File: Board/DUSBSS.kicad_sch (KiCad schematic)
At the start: 8 parts, among them Q2 BC857, U5 AP22652W6-7

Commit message: Finished Schematic
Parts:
- C2, C3: footprint (none) -> Capacitor_SMD:C_0603_1608Metric
- R19: renamed from R16; footprint (none) -> Resistor_SMD:R_0603_1608Metric
- R5, R6, R7: footprint (none) -> Resistor_SMD:R_0603_1608Metric
- U5: footprint SOIC_52W6-7_DIO -> Library:SOIC_52W6-7_DIO
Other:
- sheet USB_C0 ports: added A0, A1; removed none
- sheet USB_C1 ports: added A0, A1; removed none
- note added: "Protection and Detection"
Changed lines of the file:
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@@
 	(generator_version "9.0")
 	(paper "A4")
+	(text "Protection and Detection"
+		(exclude_from_sim no)
+		(at 152.146 155.194 0)
+		(effects
+			(font
+				(size 2.45 2.45)
+				(thickness 0.49)
+				(bold yes)
+			)
+		)
+	)
 	(junction
 		(at 125.73 125.73)
@@
 		)
 	)
+	(bus
+		(pts
+			(xy 193.04 64.77) (xy 193.04 157.48)
+		)
+		(stroke
+			(width 0)
+			(type default)
+		)
+	)
 	(wire
 		(pts
@@
 		)
 	)
+	(bus
+		(pts
+			(xy 111.76 64.77) (xy 193.04 64.77)
+		)
+		(stroke
+			(width 0)
+			(type default)
+		)
+	)
 	(wire
 		(pts
@@
 		)
 	)
+	(bus
+		(pts
+			(xy 111.76 157.48) (xy 111.76 64.77)
+		)
+		(stroke
+			(width 0)
+			(type default)
+		)
+	)
 	(wire
 		(pts
@@
 		(pts
 			(xy 153.67 102.87) (xy 153.67 130.81)
+		)
+		(stroke
+			(width 0)
+			(type default)
+		)
+	)
+	(bus
+		(pts
+			(xy 193.04 157.48) (xy 111.76 157.48)
 		)
 		(stroke
@@
 		)
 	)
+	(hierarchical_label "A10"
+		(shape bidirectional)
+		(at 186.69 128.27 0)
+		(effects
+			(font
+				(size 1.27 1.27)
+			)
+			(justify left)
+		)
+	)
 	(hierarchical_label "FAULT"
 		(shape output)
@@
 			)
 			(justify right)
+		)
+	)
+	(hierarchical_label "A01"
+		(shape bidirectional)
+		(at 186.69 97.79 0)
+		(effects
+			(font
+				(size 1.27 1.27)
+			)
+			(justify left)
+		)
+	)
+	(hierarchical_label "A11"
+		(shape bidirectional)
+		(at 186.69 125.73 0)
+		(effects
+			(font
+				(size 1.27 1.27)
+			)
+			(justify left)
+		)
+	)
+	(hierarchical_label "A00"
+		(shape bidirectional)
+		(at 186.69 100.33 0)
+		(effects
+			(font
+				(size 1.27 1.27)
+			)
+			(justify left)
 		)
 	)
@@
 			)
 		)
-		(property "Footprint" ""
+		(property "Footprint" "Resistor_SMD:R_0603_1608Metric"
 			(at 120.65 76.962 90)
 			(effects
@@
 				)
 				(path "/06ff9557-1f9b-4670-8a34-bb7684a016dd/21559adc-22f0-4da5-bb39-da22b4a6076e"
-					(reference "R10")
+					(reference "R12")
 					(unit 1)
 				)
 				(path "/06ff9557-1f9b-4670-8a34-bb7684a016dd/2b86b0ae-2209-4a30-98e5-d26e75080e9f"
-					(reference "R12")
+					(reference "R15")
 					(unit 1)
 				)
 				(path "/06ff9557-1f9b-4670-8a34-bb7684a016dd/c6b53444-adaa-455c-990e-02e7d6acd668"
-					(reference "R8")
+					(reference "R9")
 					(unit 1)
 				)
@@
 			)
 		)
-		(property "Footprint" ""
+		(property "Footprint" "Resistor_SMD:R_0603_1608Metric"
 			(at 141.732 110.49 90)
 			(effects
@@
 				)
 				(path "/06ff9557-1f9b-4670-8a34-bb7684a016dd/21559adc-22f0-4da5-bb39-da22b4a6076e"
-					(reference "R11")
+					(reference "R13")
 					(unit 1)
 				)
 				(path "/06ff9557-1f9b-4670-8a34-bb7684a016dd/2b86b0ae-2209-4a30-98e5-d26e75080e9f"
-					(reference "R13")
+					(reference "R16")
 					(unit 1)
 				)
 				(path "/06ff9557-1f9b-4670-8a34-bb7684a016dd/c6b53444-adaa-455c-990e-02e7d6acd668"
-					(reference "R9")
+					(reference "R10")
 					(unit 1)
 				)
@@
 		(dnp no)
 		(fields_autoplaced yes)
-		(property "Reference" "#PWR?"
+		(property "Reference" "#PWR0101"
 			(at 138.43 128.27 0)
 			(effects
@@
 			(project "SlimeVR_Dock"
 				(path "/06ff9557-1f9b-4670-8a34-bb7684a016dd/20608bd6-1177-4976-ba2c-965ba6250d58"
-					(reference "#PWR?")
+					(reference "#PWR0101")
 					(unit 1)
 				)
@@
 			)
 		)
-		(property "Footprint" ""
+		(property "Footprint" "Capacitor_SMD:C_0603_1608Metric"
 			(at 182.5752 88.9 0)
 			(effects
@@
 			)
 		)
-		(property "Footprint" ""
+		(property "Footprint" "Capacitor_SMD:C_0603_1608Metric"
 			(at 129.2352 93.98 0)
 			(effects
@@
 			)
 		)
-		(property "Footprint" ""
+		(property "Footprint" "Resistor_SMD:R_0603_1608Metric"
 			(at 123.952 130.81 90)
 			(effects
@@
 				)
 				(path "/06ff9557-1f9b-4670-8a34-bb7684a016dd/21559adc-22f0-4da5-bb39-da22b4a6076e"
-					(reference "R10")
+					(reference "R11")
 					(unit 1)
 				)
 				(path "/06ff9557-1f9b-4670-8a34-bb7684a016dd/2b86b0ae-2209-4a30-98e5-d26e75080e9f"
-					(reference "R11")
+					(reference "R14")
 					(unit 1)
 				)
@@
 		(on_board yes)
 		(dnp no)
-		(property "Reference" "R16"
+		(property "Reference" "R19"
 			(at 135.128 146.05 0)
 			(effects
@@
 			)
 		)
-		(property "Footprint" ""
+		(property "Footprint" "Resistor_SMD:R_0603_1608Metric"
 			(at 139.192 147.32 90)
 			(effects
@@
 			(project "SlimeVR_Dock"
 				(path "/06ff9557-1f9b-4670-8a34-bb7684a016dd/20608bd6-1177-4976-ba2c-965ba6250d58"
-					(reference "R16")
+					(reference "R19")
 					(unit 1)
 				)
 				(path "/06ff9557-1f9b-4670-8a34-bb7684a016dd/21559adc-22f0-4da5-bb39-da22b4a6076e"
-					(reference "R18")
+					(reference "R21")
 					(unit 1)
 				)
 				(path "/06ff9557-1f9b-4670-8a34-bb7684a016dd/2b86b0ae-2209-4a30-98e5-d26e75080e9f"
-					(reference "R19")
+					(reference "R22")
 					(unit 1)
 				)
 				(path "/06ff9557-1f9b-4670-8a34-bb7684a016dd/c6b53444-adaa-455c-990e-02e7d6acd668"
-					(reference "R17")
+					(reference "R20")
 					(unit 1)
 				)
@@
 			)
 		)
-		(property "Footprint" "SOIC_52W6-7_DIO"
+		(property "Footprint" "Library:SOIC_52W6-7_DIO"
 			(at 170.18 81.28 0)
 			(effects
@@
 		(on_board yes)
 		(dnp no)
-		(property "Reference" "#PWR?"
+		(property "Reference" "#PWR0102"
 			(at 143.51 110.49 0)
 			(effects
@@
 			(project "SlimeVR_Dock"
 				(path "/06ff9557-1f9b-4670-8a34-bb7684a016dd/20608bd6-1177-4976-ba2c-965ba6250d58"
-					(reference "#PWR?")
+					(reference "#PWR0102")
 					(unit 1)
 				)
 				(path "/06ff9557-1f9b-4670-8a34-bb7684a016dd/21559adc-22f0-4da5-bb39-da22b4a6076e"
-					(reference "#PWR?")
+					(reference "#PWR0105")
 					(unit 1)
 				)
 				(path "/06ff9557-1f9b-4670-8a34-bb7684a016dd/2b86b0ae-2209-4a30-98e5-d26e75080e9f"
-					(reference "#PWR?")
+					(reference "#PWR0106")
 					(unit 1)
 				)
 				(path "/06ff9557-1f9b-4670-8a34-bb7684a016dd/c6b53444-adaa-455c-990e-02e7d6acd668"
-					(reference "#PWR?")
+					(reference "#PWR0104")
 					(unit 1)
 				)
@@
 		(on_board yes)
 		(dnp no)
-		(property "Reference" "#PWR?"
+		(property "Reference" "#PWR0103"
 			(at 173.99 90.17 0)
 			(effects
@@
 			(project "SlimeVR_Dock"
 				(path "/06ff9557-1f9b-4670-8a34-bb7684a016dd/20608bd6-1177-4976-ba2c-965ba6250d58"
-					(reference "#PWR?")
+					(reference "#PWR0103")
 					(unit 1)
 				)
@@
 			)
 		)
+		(pin "A1" bidirectional
+			(at 186.69 125.73 0)
+			(effects
+				(font
+					(size 1.27 1.27)
+				)
+				(justify right)
+			)
+		)
+		(pin "A0" bidirectional
+			(at 186.69 128.27 0)
+			(effects
+				(font
+					(size 1.27 1.27)
+				)
+				(justify right)
+			)
+		)
 		(instances
 			(project "SlimeVR_Dock"
@@
 			)
 		)
+		(pin "A1" bidirectional
+			(at 186.69 97.79 0)
+			(effects
+				(font
+					(size 1.27 1.27)
+				)
+				(justify right)
+			)
+		)
+		(pin "A0" bidirectional
+			(at 186.69 100.33 0)
+			(effects
+				(font
+					(size 1.27 1.27)
+				)
+				(justify right)
+			)
+		)

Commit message: Updated fields for LCSC
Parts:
- Q2: LCSC (none) -> C111644
- U5: LCSC (none) -> C2158038
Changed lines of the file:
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@@
+			)
+		)
+		(property "LCSC" "C111644"
+			(at 132.08 128.27 90)
+			(effects
+				(font
+					(size 1.27 1.27)
+				)
+				(hide yes)
 			)
 		)
@@
 			(at 170.18 81.28 0)
 			(effects
+				(font
+					(size 1.27 1.27)
+				)
+				(hide yes)
+			)
+		)
+		(property "LCSC" "C2158038"
+			(at 170.18 81.28 0)
+			(effects

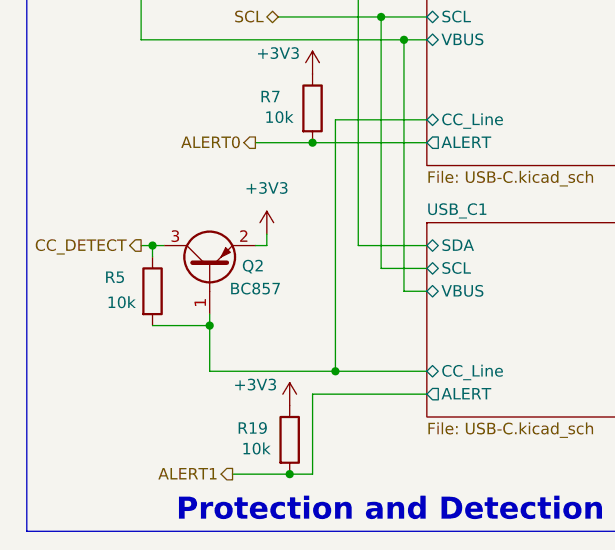
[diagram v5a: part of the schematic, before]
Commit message: Fixed CC_detect transistor
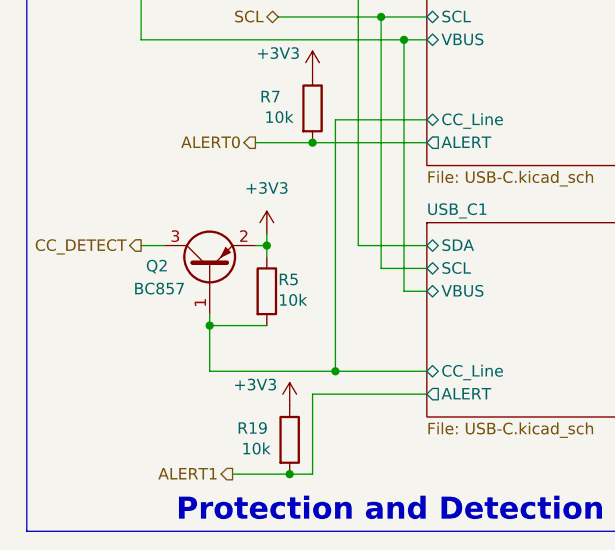
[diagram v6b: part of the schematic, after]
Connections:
- net +3V3: now also R5.1
- net CC_DETECT: no longer R5.1
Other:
- moved on the sheet: R5
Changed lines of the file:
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@@
 	)
 	(junction
-		(at 125.73 125.73)
+		(at 138.43 125.73)
 		(diameter 0)
 		(color 0 0 0 0)
@@
 	)
 	(junction
+		(at 132.08 134.62)
+		(diameter 0)
+		(color 0 0 0 0)
+	)
+	(junction
 		(at 143.51 114.3)
 		(diameter 0)
@@
 		(color 0 0 0 0)
 	)
-	(junction
-		(at 132.08 134.62)
-		(diameter 0)
-		(color 0 0 0 0)
-	)
 	(wire
 		(pts
@@
 	(wire
 		(pts
-			(xy 124.46 125.73) (xy 125.73 125.73)
-		)
-		(stroke
-			(width 0)
-			(type default)
-		)
-	)
-	(wire
-		(pts
-			(xy 132.08 134.62) (xy 132.08 133.35)
+			(xy 132.08 133.35) (xy 132.08 134.62)
 		)
 		(stroke
@@
 	(wire
 		(pts
+			(xy 132.08 134.62) (xy 138.43 134.62)
+		)
+		(stroke
+			(width 0)
+			(type default)
+		)
+	)
+	(wire
+		(pts
 			(xy 170.18 81.28) (xy 181.61 81.28)
 		)
@@
 	(wire
 		(pts
+			(xy 138.43 125.73) (xy 138.43 127)
+		)
+		(stroke
+			(width 0)
+			(type default)
+		)
+	)
+	(wire
+		(pts
 			(xy 148.59 97.79) (xy 156.21 97.79)
 		)
@@
 	(wire
 		(pts
-			(xy 125.73 125.73) (xy 127 125.73)
+			(xy 124.46 125.73) (xy 127 125.73)
 		)
 		(stroke
@@
 	(wire
 		(pts
-			(xy 125.73 134.62) (xy 132.08 134.62)
-		)
-		(stroke
-			(width 0)
-			(type default)
-		)
-	)
-	(wire
-		(pts
 			(xy 182.88 81.28) (xy 181.61 81.28)
-		)
-		(stroke
-			(width 0)
-			(type default)
-		)
-	)
-	(wire
-		(pts
-			(xy 125.73 127) (xy 125.73 125.73)
 		)
 		(stroke
@@
 	(symbol
 		(lib_id "Device:R")
-		(at 125.73 130.81 0)
+		(at 138.43 130.81 0)
 		(unit 1)
 		(exclude_from_sim no)
@@
 		(dnp no)
 		(property "Reference" "R5"
-			(at 120.396 129.286 0)
+			(at 139.7 129.54 0)
 			(effects
 				(font
@@
 		)
 		(property "Value" "10k"
-			(at 120.65 132.08 0)
+			(at 139.7 131.826 0)
 			(effects
 				(font
@@
 		)
 		(property "Footprint" "Resistor_SMD:R_0603_1608Metric"
-			(at 123.952 130.81 90)
+			(at 136.652 130.81 90)
 			(effects
 				(font
@@
 		)
 		(property "Datasheet" "~"
-			(at 125.73 130.81 0)
+			(at 138.43 130.81 0)
 			(effects
 				(font
@@
 		)
 		(property "Description" "Resistor"
-			(at 125.73 130.81 0)
+			(at 138.43 130.81 0)
 			(effects
 				(font
@@
 		(dnp no)
 		(property "Reference" "Q2"
-			(at 136.906 128.016 90)
+			(at 126.238 128.016 90)
 			(effects
 				(font
@@
 		)
 		(property "Value" "BC857"
-			(at 137.16 130.556 90)
-			(effects
-				(font
+			(at 126.492 130.556 90)
+			(effects
+				(font

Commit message: Version 3
Hopefully it works idk ?:D
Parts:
- added R38, R46, R50: 10k, Resistor_SMD:R_0603_1608Metric, symbol Device:R
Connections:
- net +3V3: now also R46.1
- net CC_DETECT: now also R38.2
- net EN: now also R50.2
- net Earth: now also R38.1, R50.1
- net FAULT: now also R46.2
